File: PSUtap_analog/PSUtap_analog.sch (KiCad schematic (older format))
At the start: 58 parts, among them J1 Conn_to_digital_board, U1 AD7708, U2 LT6105, U3 LT6105, U4 LT6105, U5 LT6105, U6 LT6105

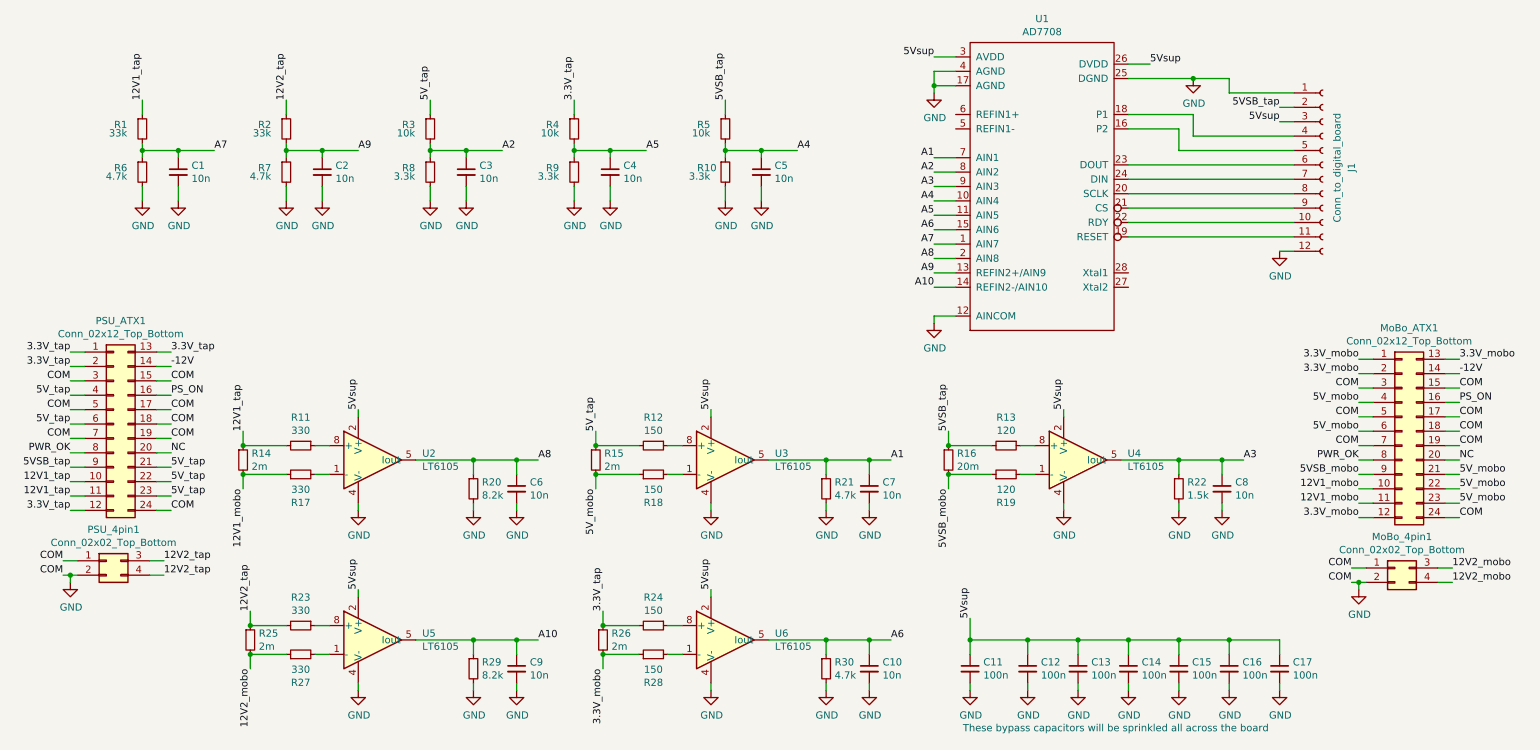
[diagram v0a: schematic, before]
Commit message: Updated analog board PCB and started digital board PSB
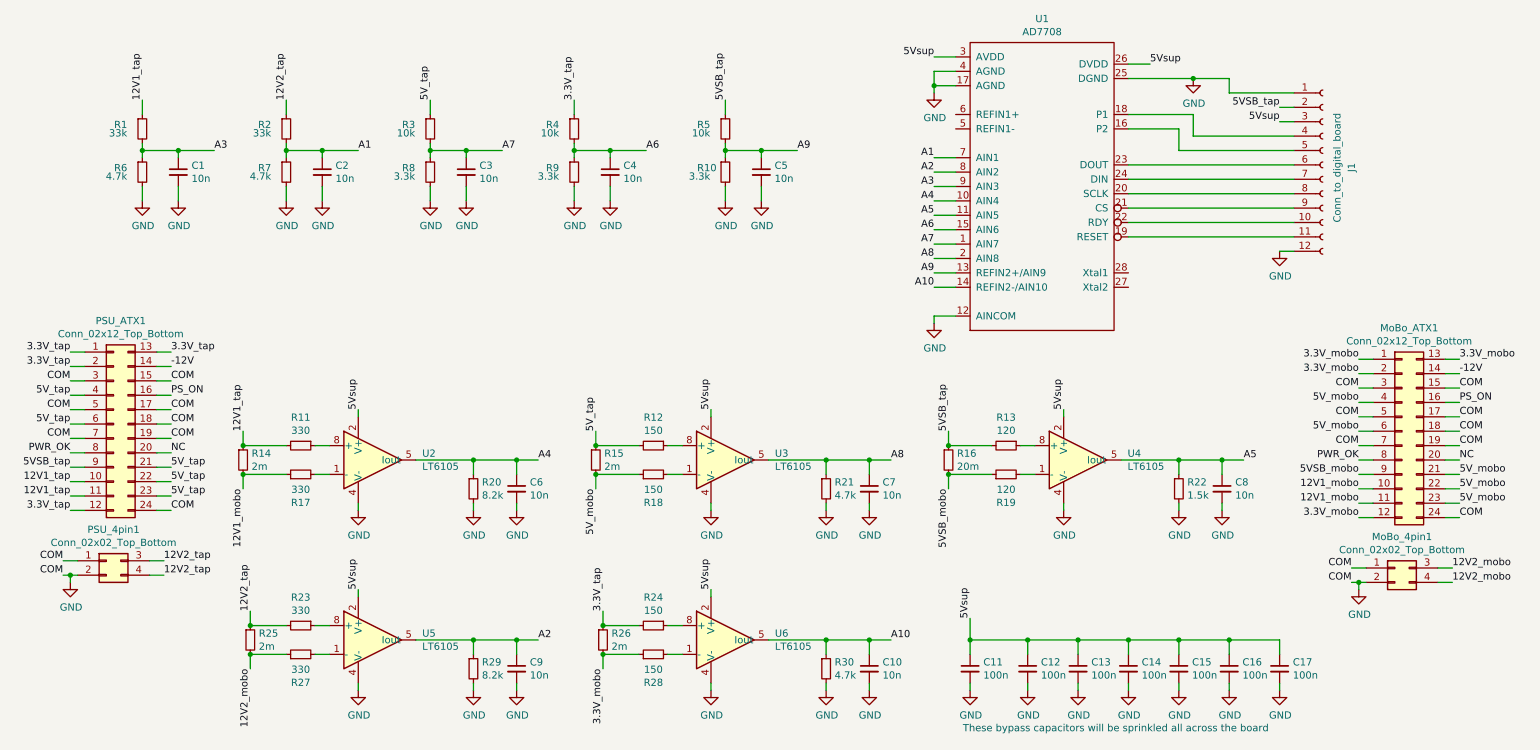
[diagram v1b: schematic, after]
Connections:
- net A1: now also C2.1, R2.2, R7.1; no longer C7.1, R21.1, U3.5 (Iout)
- net A10: now also C10.1, R30.1, U6.5 (Iout); no longer C9.1, R29.1, U5.5 (Iout)
- net A2: now also C9.1, R29.1, U5.5 (Iout); no longer C3.1, R3.2, R8.1
- net A3: now also C1.1, R1.2, R6.1; no longer C8.1, R22.1, U4.5 (Iout)
- net A4: now also C6.1, R20.1, U2.5 (Iout); no longer C5.1, R10.1, R5.2
- net A5: now also C8.1, R22.1, U4.5 (Iout); no longer C4.1, R4.2, R9.1
- net A6: now also C4.1, R4.2, R9.1; no longer C10.1, R30.1, U6.5 (Iout)
- net A7: now also C3.1, R3.2, R8.1; no longer C1.1, R1.2, R6.1
- net A8: now also C7.1, R21.1, U3.5 (Iout); no longer C6.1, R20.1, U2.5 (Iout)
- net A9: now also C5.1, R10.1, R5.2; no longer C2.1, R2.2, R7.1
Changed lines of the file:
@@
 A10
 Text Label 2000 1650 0    50   ~ 0
-A7
+A3
 Text Label 5000 1650 0    50   ~ 0
-A5
+A6
 Text Label 6050 1650 0    50   ~ 0
-A4
+A9
 $Comp
 L Device:R_Small R5
@@
 $EndComp
 Text Label 4250 3800 0    50   ~ 0
-A8
+A4
 Text Label 4250 5050 0    50   ~ 0
+A2
+Text Label 6700 5050 0    50   ~ 0
 A10
-Text Label 6700 5050 0    50   ~ 0
-A6
 Text Label 9150 3800 0    50   ~ 0
-A3
+A5
 Wire Wire Line
 	7000 1700 7150 1700
@@
 	9050 5050 8700 5050
 Text Label 6700 3800 0    50   ~ 0
+A8
+Text Label 3000 1650 0    50   ~ 0
 A1
-Text Label 3000 1650 0    50   ~ 0
-A9
 Text Label 4000 1650 0    50   ~ 0
-A2
+A7
 Wire Wire Line
 	9500 1250 9050 1250

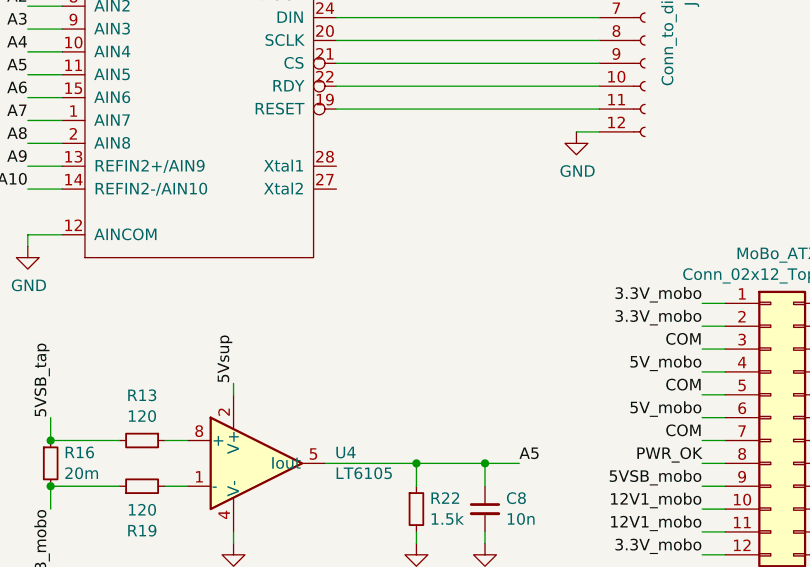
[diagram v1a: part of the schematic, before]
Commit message: Removed PCB copies, added xtal to ADC in analog board, finished digital board's PCB
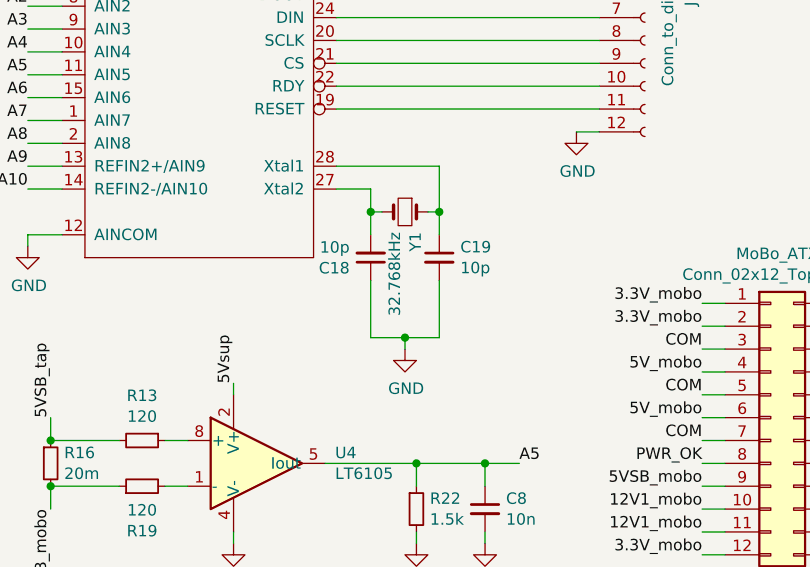
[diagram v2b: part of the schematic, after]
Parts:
- added C18, C19: 10p, Capacitor_SMD:C_0603_1608Metric_Pad1.05x0.95mm_HandSolder, symbol Device:C_Small
- added Y1: 32.768kHz, Crystal:Crystal_SMD_EuroQuartz_EQ161-2Pin_3.2x1.5mm_HandSoldering, symbol Device:Crystal_Small
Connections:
- net GND: now also C18.1, C19.2
- net at U1.27 (Xtal2): now also C18.2, Y1.2
- net at U1.28 (Xtal1): now also C19.1, Y1.1
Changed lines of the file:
@@
 	8800 1150 9050 1150
 Connection ~ 8800 1150
+$Comp
+L Device:Crystal_Small Y1
+U 1 1 5FAE7149
+P 8650 2700
+F 0 "Y1" V 8604 2788 50  0000 L CNN
+F 1 "32.768kHz" V 8695 2788 50  0000 L CNN
+F 2 "Crystal:Crystal_SMD_EuroQuartz_EQ161-2Pin_3.2x1.5mm_HandSoldering" H 8650 2700 50  0001 C CNN
+F 3 "https://eu.mouser.com/datasheet/2/530/cm7v-t1a-1085727.pdf" H 8650 2700 50  0001 C CNN
+	1    8650 2700
+	-1   0    0    1
+$EndComp
+$Comp
+L Device:C_Small C19
+U 1 1 5FC7C068
+P 8800 2900
+F 0 "C19" H 8892 2946 50  0000 L CNN
+F 1 "10p" H 8892 2855 50  0000 L CNN
+F 2 "Capacitor_SMD:C_0603_1608Metric_Pad1.05x0.95mm_HandSolder" H 8800 2900 50  0001 C CNN
+F 3 "~" H 8800 2900 50  0001 C CNN
+	1    8800 2900
+	1    0    0    -1
+$EndComp
+$Comp
+L Device:C_Small C18
+U 1 1 5FC7FDCA
+P 8500 2900
+F 0 "C18" H 8592 2946 50  0000 L CNN
+F 1 "10p" H 8592 2855 50  0000 L CNN
+F 2 "Capacitor_SMD:C_0603_1608Metric_Pad1.05x0.95mm_HandSolder" H 8500 2900 50  0001 C CNN
+F 3 "~" H 8500 2900 50  0001 C CNN
+	1    8500 2900
+	-1   0    0    1
+$EndComp
+Wire Wire Line
+	8350 2600 8500 2600
+Wire Wire Line
+	8500 2600 8500 2700
+Wire Wire Line
+	8550 2700 8500 2700
+Connection ~ 8500 2700
+Wire Wire Line
+	8500 2700 8500 2800
+Wire Wire Line
+	8800 2500 8800 2700
+Wire Wire Line
+	8800 2700 8750 2700
+Wire Wire Line
+	8350 2500 8800 2500
+Wire Wire Line
+	8800 2700 8800 2800
+Connection ~ 8800 2700
+Wire Wire Line
+	8800 3000 8800 3250
+Wire Wire Line
+	8800 3250 8650 3250
+Wire Wire Line
+	8500 3250 8500 3000
+$Comp
+L power:GND #PWR037
+U 1 1 5FCD8763
+P 8650 3300
+F 0 "#PWR037" H 8650 3050 50  0001 C CNN
+F 1 "GND" H 8655 3127 50  0000 C CNN
+F 2 "" H 8650 3300 50  0001 C CNN
+F 3 "" H 8650 3300 50  0001 C CNN
+	1    8650 3300
+	1    0    0    -1
+$EndComp
+Wire Wire Line
+	8650 3300 8650 3250
+Connection ~ 8650 3250
+Wire Wire Line
+	8650 3250 8500 3250
 $EndSCHEMATC

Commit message: updated kicad projects caches
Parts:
- U1: symbol Analog_ADC:AD7708 -> PSUtap_analog-rescue:AD7708-Analog_ADC
- U2, U3, U4, U5, U6: symbol Amplifier_Current:LT6105 -> PSUtap_analog-rescue:LT6105-Amplifier_Current
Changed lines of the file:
@@
 $EndComp
 $Comp
-L Analog_ADC:AD7708 U1
+L PSUtap_analog-rescue:AD7708-Analog_ADC U1
 U 1 1 5EB8BD75
 P 7750 1900
@@
 Connection ~ 3800 5050
 $Comp
-L Amplifier_Current:LT6105 U2
+L PSUtap_analog-rescue:LT6105-Amplifier_Current U2
 U 1 1 5EDFB0C9
 P 3100 3800
@@
 $EndComp
 $Comp
-L Amplifier_Current:LT6105 U3
+L PSUtap_analog-rescue:LT6105-Amplifier_Current U3
 U 1 1 5EDFC037
 P 5550 3800
@@
 $EndComp
 $Comp
-L Amplifier_Current:LT6105 U6
+L PSUtap_analog-rescue:LT6105-Amplifier_Current U6
 U 1 1 5EDFC763
 P 5550 5050
@@
 $EndComp
 $Comp
-L Amplifier_Current:LT6105 U4
+L PSUtap_analog-rescue:LT6105-Amplifier_Current U4
 U 1 1 5EDFCB68
 P 8000 3800
@@
 	5450 4750 5450 4700
 $Comp
-L Amplifier_Current:LT6105 U5
+L PSUtap_analog-rescue:LT6105-Amplifier_Current U5
 U 1 1 5EDFBA9E
 P 3100 5050
